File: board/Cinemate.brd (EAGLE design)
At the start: 39.5 x 14.8 mm, 7 parts, among them J1 AVR_SPI_PROG_3X2PTH, P1 DE9-PCB-EDGEMALE, P2 DE9-PCB-EDGEFEMALE, U1 ATTINY85-20PU

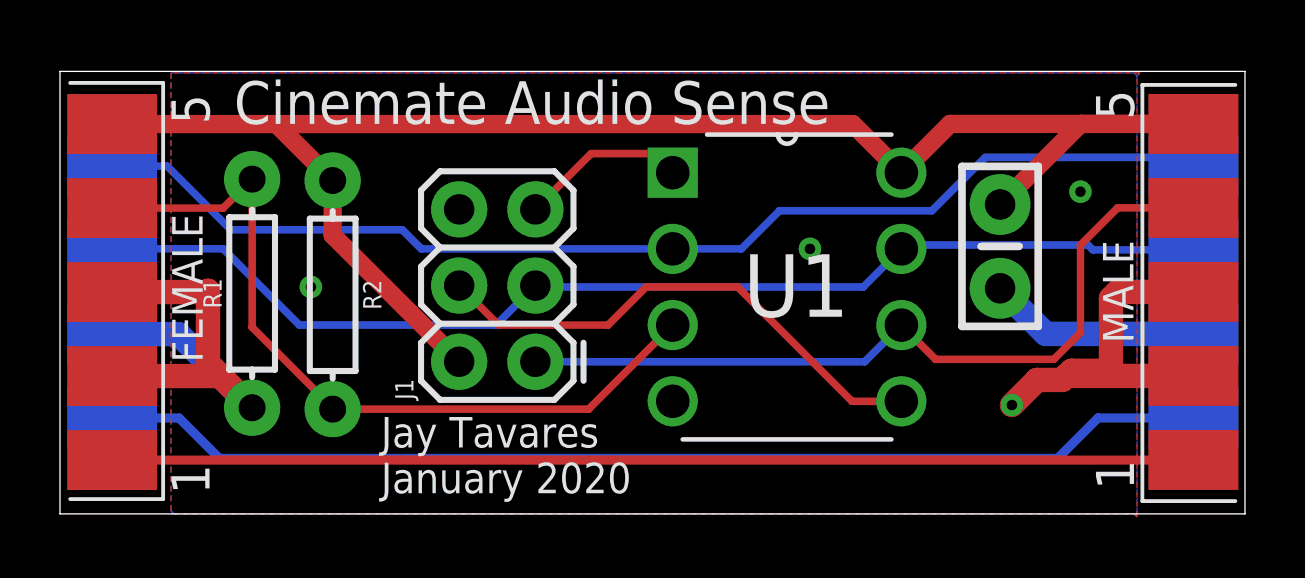
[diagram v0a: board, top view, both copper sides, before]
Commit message: Update board & ignore .vscode
Reduce length of board by 1 mm to allow for a better fit in the enclosure
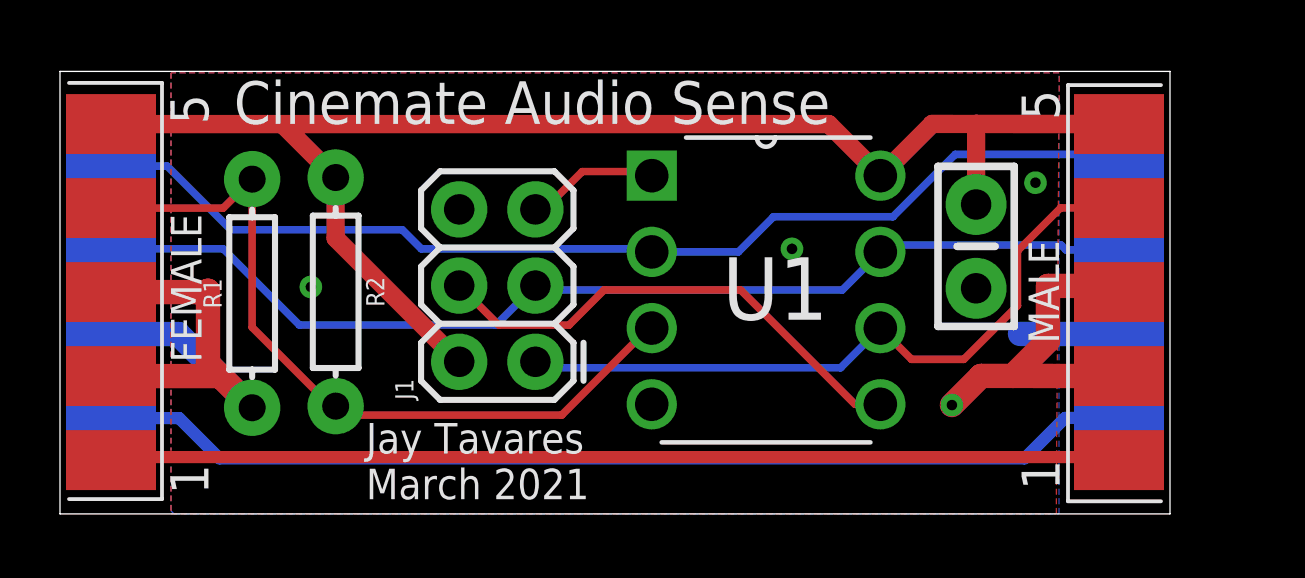
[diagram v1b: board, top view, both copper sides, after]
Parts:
- moved P1 2.48 mm to (35.3, 7.39)
- moved C1 0.80 mm to (30.5, 8.92)
- moved U1 0.71 mm to (27.3, 3.65)
- moved R2 0.14 mm to (9.19, 7.40)
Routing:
- net GND: track 38.8 -> 33.8 mm
- net CTRL_OUT: track 26.7 -> 23.7 mm
- net VCC: track 55.4 -> 52.8 mm
- net ANALOG_LEFT+: track 37.2 -> 34.7 mm
- net ANALOG_RIGHT+: track 36.0 -> 33.7 mm
- net OPTICAL_AUDIO: track 38.3 -> 36.0 mm
- net IR: track 38.6 -> 36.3 mm
- net RST: track 5.61 -> 4.46 mm
- net MOSI: track 17.4 -> 16.6 mm
- net CTRL_IN: track 26.3 -> 25.8 mm
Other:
- board size 39.5 x 14.8 mm -> 37 x 14.8 mm
- board text added: "Jay Tavares March 2021"
- board text removed: "Jay Tavares January 2020"
